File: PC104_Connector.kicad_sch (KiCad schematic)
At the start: 2 parts

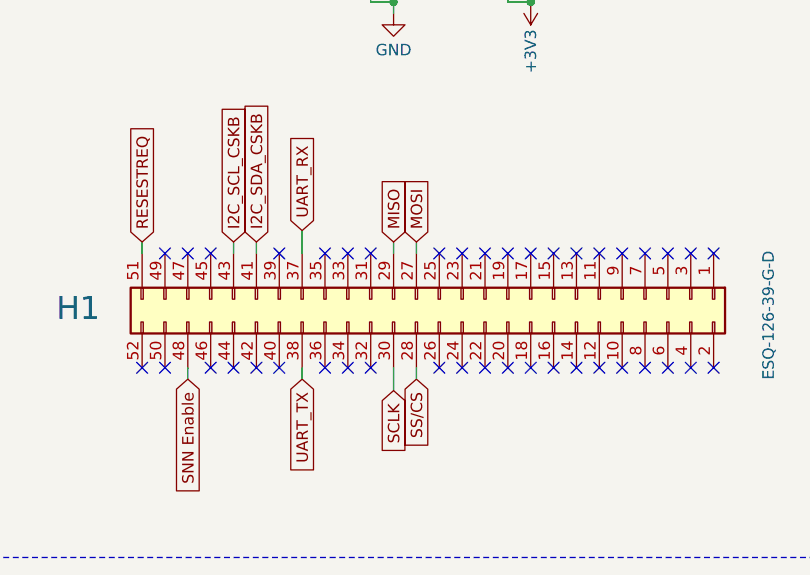
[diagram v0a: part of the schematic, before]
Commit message: Removed SPI Connections
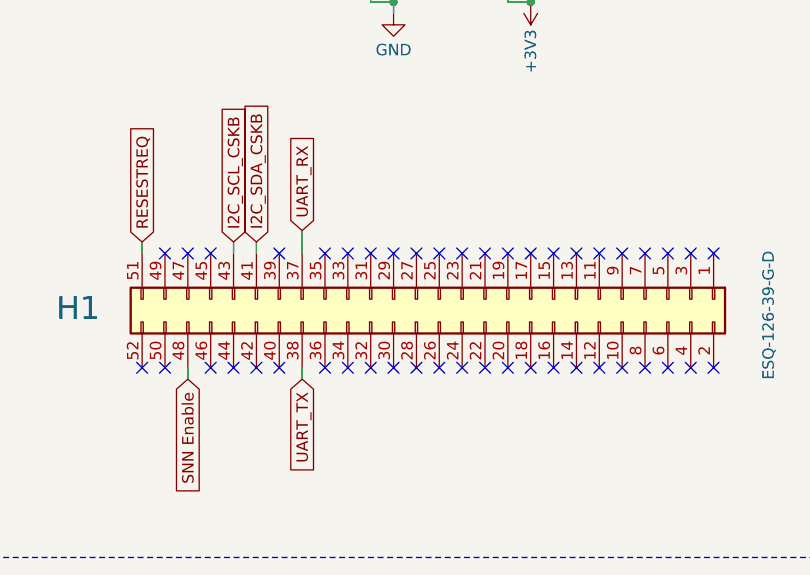
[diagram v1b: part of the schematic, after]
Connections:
- net MISO: no longer names the net of H1.29 (Pin_29)
- net MOSI: no longer names the net of H1.27 (Pin_27)
- net SCLK: no longer names the net of H1.30 (Pin_30)
- net SS/CS: no longer names the net of H1.28 (Pin_28)
- no-connect marks 88 -> 92
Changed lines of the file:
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@@
+	)
+	(no_connect
+		(at 149.86 100.33)
 	)
 	(no_connect
@@
 	)
 	(no_connect
+		(at 149.86 113.03)
+	)
+	(no_connect
 		(at 175.26 58.42)
 	)
@@
 	)
 	(no_connect
+		(at 147.32 113.03)
+	)
+	(no_connect
 		(at 172.72 58.42)
 	)
@@
 	)
 	(no_connect
+		(at 147.32 100.33)
+	)
+	(no_connect
 		(at 167.64 71.12)
 	)
@@
 	(wire
 		(pts
-			(xy 147.32 115.57) (xy 147.32 113.03)
-		)
-		(stroke
-			(width 0)
-			(type default)
-		)
-	)
-	(wire
-		(pts
 			(xy 132.08 99.06) (xy 132.08 100.33)
 		)
@@
 	(wire
 		(pts
-			(xy 149.86 114.3) (xy 149.86 113.03)
-		)
-		(stroke
-			(width 0)
-			(type default)
-		)
-	)
-	(wire
-		(pts
-			(xy 147.32 99.06) (xy 147.32 100.33)
-		)
-		(stroke
-			(width 0)
-			(type default)
-		)
-	)
-	(wire
-		(pts
 			(xy 137.16 97.79) (xy 137.16 100.33)
 		)
@@
 	(wire
 		(pts
-			(xy 149.86 99.06) (xy 149.86 100.33)
-		)
-		(stroke
-			(width 0)
-			(type default)
-		)
-	)
-	(wire
-		(pts
 			(xy 147.32 72.39) (xy 147.32 71.12)
 		)
@@
 		)
 	)
-	(global_label "MOSI"
-		(shape input)
-		(at 149.86 99.06 90)
+	(global_label "I2C_SDA_CSKB"
+		(shape input)
+		(at 132.08 99.06 90)
 		(fields_autoplaced yes)
 		(effects
@@
 		)
 		(property "Intersheetrefs" "${INTERSHEET_REFS}"
-			(at 149.86 91.4786 90)
+			(at 132.08 82.4677 90)
 			(effects
 				(font
@@
 		)
 	)
-	(global_label "I2C_SDA_CSKB"
-		(shape input)
-		(at 132.08 99.06 90)
+	(global_label "RESESTREQ"
+		(shape input)
+		(at 119.38 99.06 90)
 		(fields_autoplaced yes)
 		(effects
@@
 		)
 		(property "Intersheetrefs" "${INTERSHEET_REFS}"
-			(at 132.08 82.4677 90)
+			(at 119.38 85.3707 90)
 			(effects
 				(font
@@
 		)
 	)
-	(global_label "RESESTREQ"
-		(shape input)
-		(at 119.38 99.06 90)
+	(global_label "UART_RX"
+		(shape input)
+		(at 137.16 97.79 90)
 		(fields_autoplaced yes)
 		(effects
@@
 		)
 		(property "Intersheetrefs" "${INTERSHEET_REFS}"
-			(at 119.38 85.3707 90)
+			(at 137.16 86.701 90)
 			(effects
 				(font
@@
 		)
 	)
-	(global_label "UART_RX"
-		(shape input)
-		(at 137.16 97.79 90)
-		(fields_autoplaced yes)
-		(effects
-			(font
-				(size 1.27 1.27)
-			)
-			(justify left)
-		)
-		(property "Intersheetrefs" "${INTERSHEET_REFS}"
-			(at 137.16 86.701 90)
-			(effects
-				(font
-					(size 1.27 1.27)
-				)
-				(justify left)
-				(hide yes)
-			)
-		)
-	)
 	(global_label "UART_TX"
 		(shape input)
@@
 			(effects
 				(font
-					(size 1.27 1.27)
-				)
-				(justify right)
-				(hide yes)
-			)
-		)
-	)
-	(global_label "SCLK"
-		(shape input)
-		(at 147.32 115.57 270)
-		(fields_autoplaced yes)
-		(effects
-			(font
-				(size 1.27 1.27)
-			)
-			(justify right)
-		)
-		(property "Intersheetrefs" "${INTERSHEET_REFS}"
-			(at 147.32 123.3328 90)
-			(effects
-				(font
-					(size 1.27 1.27)
-				)
-				(justify right)
-				(hide yes)
-			)
-		)
-	)
-	(global_label "MISO"
-		(shape input)
-		(at 147.32 99.06 90)
-		(fields_autoplaced yes)
-		(effects
-			(font
-				(size 1.27 1.27)
-			)
-			(justify left)
-		)
-		(property "Intersheetrefs" "${INTERSHEET_REFS}"
-			(at 147.32 91.4786 90)
-			(effects
-				(font
-					(size 1.27 1.27)
-				)
-				(justify left)
-				(hide yes)
-			)
-		)
-	)
-	(global_label "SS{slash}CS"
-		(shape input)
-		(at 149.86 114.3 270)
-		(fields_autoplaced yes)
-		(effects
-			(font
-				(size 1.27 1.27)
-			)
-			(justify right)
-		)
-		(property "Intersheetrefs" "${INTERSHEET_REFS}"
-			(at 149.86 123.5142 90)
-			(effects
-				(font

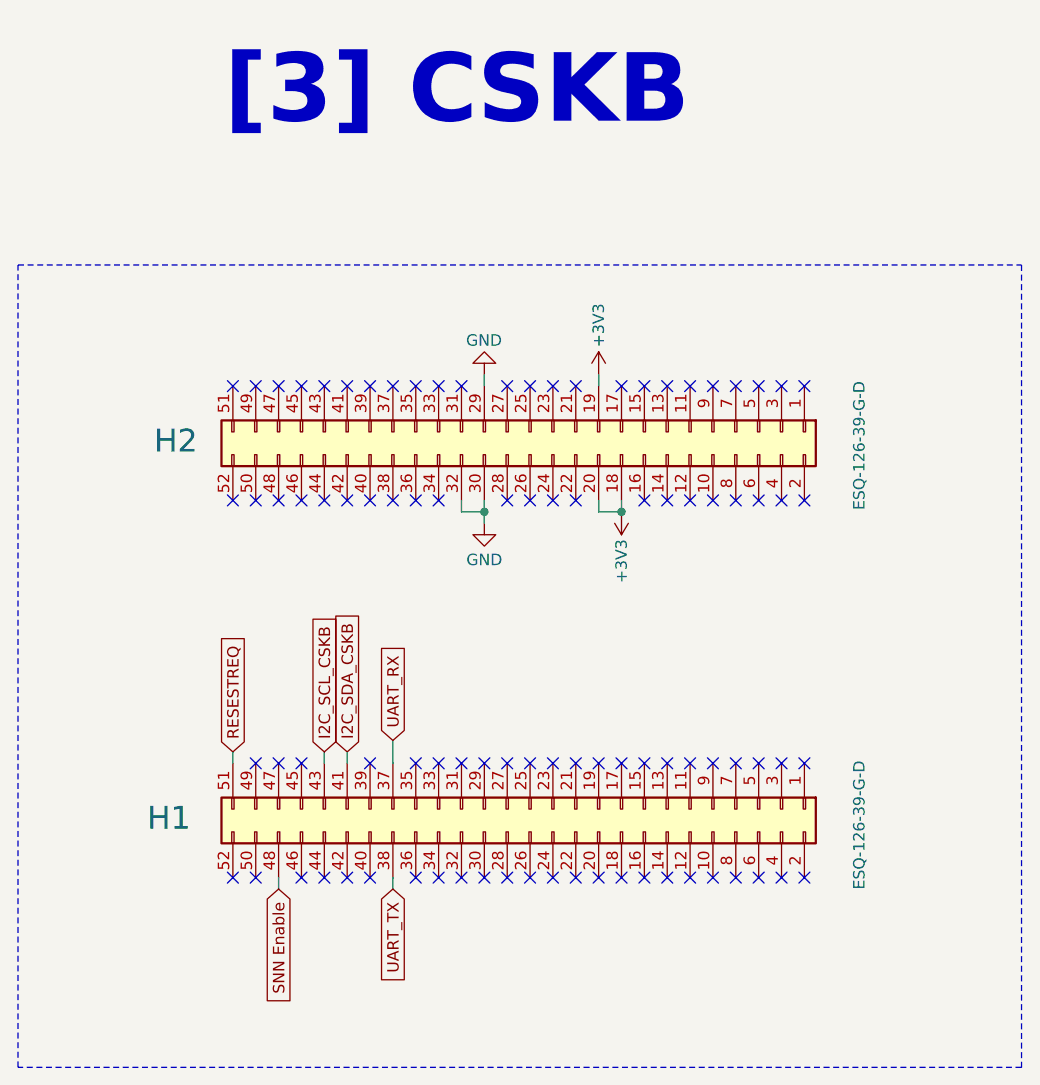
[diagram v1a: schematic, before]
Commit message: Added hierarchical lables to the schematic
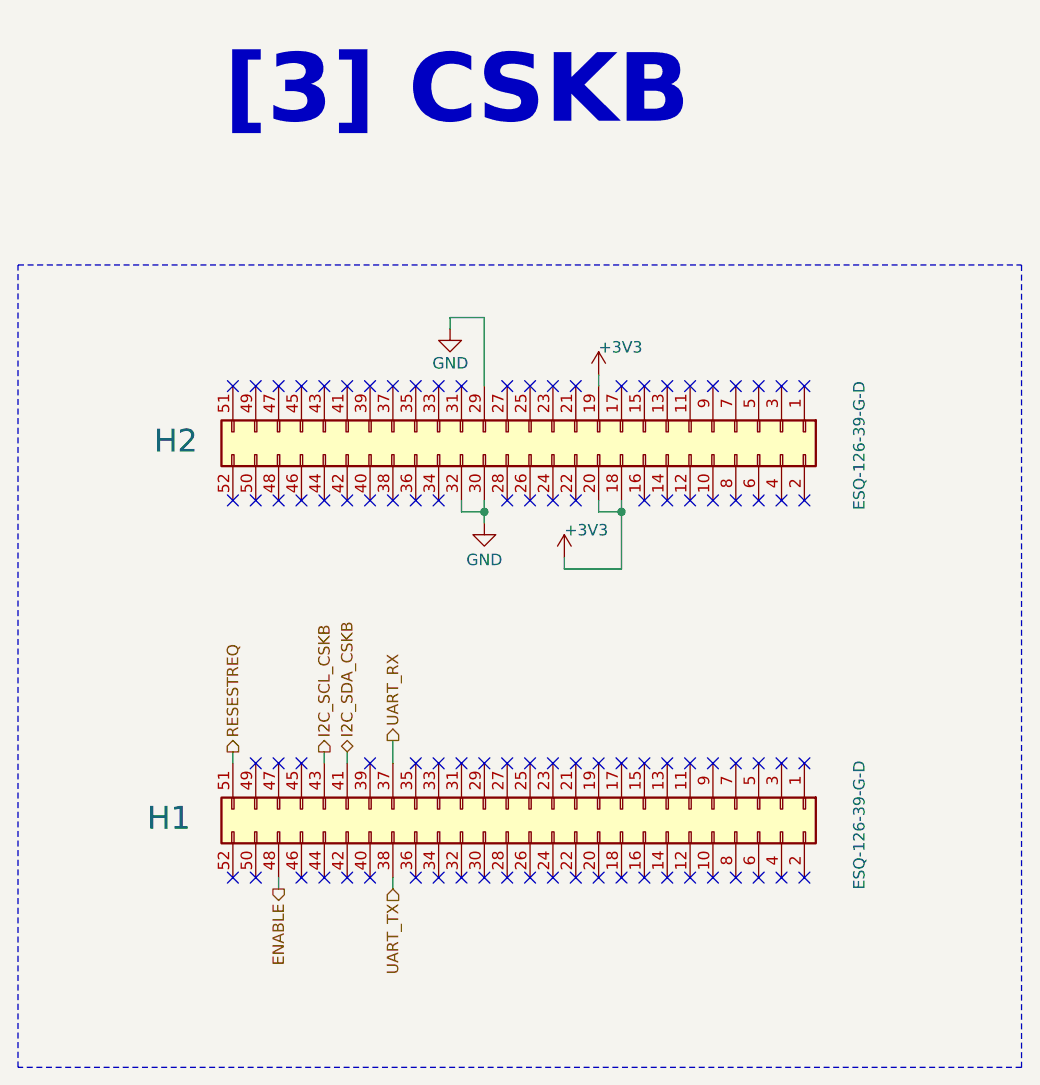
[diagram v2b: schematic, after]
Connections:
- net SNN Enable renamed ENABLE
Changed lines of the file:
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@@
+	(wire
+		(pts
+			(xy 147.32 50.8) (xy 147.32 58.42)
+		)
+		(stroke
+			(width 0)
+			(type default)
+		)
+	)
 	(wire
 		(pts
@@
 	(wire
 		(pts
+			(xy 143.51 50.8) (xy 147.32 50.8)
+		)
+		(stroke
+			(width 0)
+			(type default)
+		)
+	)
+	(wire
+		(pts
 			(xy 124.46 114.3) (xy 124.46 113.03)
 		)
@@
 	(wire
 		(pts
+			(xy 156.21 77.47) (xy 156.21 78.74)
+		)
+		(stroke
+			(width 0)
+			(type default)
+		)
+	)
+	(wire
+		(pts
 			(xy 129.54 99.06) (xy 129.54 100.33)
 		)
@@
 	(wire
 		(pts
-			(xy 147.32 57.15) (xy 147.32 58.42)
+			(xy 143.51 52.07) (xy 143.51 50.8)
 		)
 		(stroke
@@
 	(wire
 		(pts
+			(xy 162.56 78.74) (xy 162.56 72.39)
+		)
+		(stroke
+			(width 0)
+			(type default)
+		)
+	)
+	(wire
+		(pts
+			(xy 156.21 78.74) (xy 162.56 78.74)
+		)
+		(stroke
+			(width 0)
+			(type default)
+		)
+	)
+	(wire
+		(pts
 			(xy 147.32 72.39) (xy 144.78 72.39)
 		)
@@
 		)
 	)
-	(global_label "I2C_SCL_CSKB"
-		(shape input)
-		(at 129.54 99.06 90)
-		(fields_autoplaced yes)
+	(hierarchical_label "I2C_SDA_CSKB"
+		(shape bidirectional)
+		(at 132.08 99.06 90)
 		(effects
 			(font
@@
 			(justify left)
 		)
-		(property "Intersheetrefs" "${INTERSHEET_REFS}"
-			(at 129.54 82.5282 90)
-			(effects
-				(font
-					(size 1.27 1.27)
-				)
-				(justify left)
-				(hide yes)
-			)
-		)
-	)
-	(global_label "I2C_SDA_CSKB"
-		(shape input)
-		(at 132.08 99.06 90)
-		(fields_autoplaced yes)
-		(effects
-			(font
-				(size 1.27 1.27)
-			)
-			(justify left)
-		)
-		(property "Intersheetrefs" "${INTERSHEET_REFS}"
-			(at 132.08 82.4677 90)
-			(effects
-				(font
-					(size 1.27 1.27)
-				)
-				(justify left)
-				(hide yes)
-			)
-		)
-	)
-	(global_label "RESESTREQ"
-		(shape input)
-		(at 119.38 99.06 90)
-		(fields_autoplaced yes)
-		(effects
-			(font
-				(size 1.27 1.27)
-			)
-			(justify left)
-		)
-		(property "Intersheetrefs" "${INTERSHEET_REFS}"
-			(at 119.38 85.3707 90)
-			(effects
-				(font
-					(size 1.27 1.27)
-				)
-				(justify left)
-				(hide yes)
-			)
-		)
-	)
-	(global_label "UART_RX"
-		(shape input)
-		(at 137.16 97.79 90)
-		(fields_autoplaced yes)
-		(effects
-			(font
-				(size 1.27 1.27)
-			)
-			(justify left)
-		)
-		(property "Intersheetrefs" "${INTERSHEET_REFS}"
-			(at 137.16 86.701 90)
-			(effects
-				(font
-					(size 1.27 1.27)
-				)
-				(justify left)
-				(hide yes)
-			)
-		)
-	)
-	(global_label "UART_TX"
+	)
+	(hierarchical_label "UART_TX"
 		(shape input)
 		(at 137.16 114.3 270)
-		(fields_autoplaced yes)
 		(effects
 			(font
@@
 			(justify right)
 		)
-		(property "Intersheetrefs" "${INTERSHEET_REFS}"
-			(at 137.16 125.0866 90)
-			(effects
-				(font
-					(size 1.27 1.27)
-				)
-				(justify right)
-				(hide yes)
-			)
-		)
-	)
-	(global_label "SNN Enable"
-		(shape input)
+	)
+	(hierarchical_label "RESESTREQ"
+		(shape output)
+		(at 119.38 99.06 90)
+		(effects
+			(font
+				(size 1.27 1.27)
+			)
+			(justify left)
+		)
+	)
+	(hierarchical_label "I2C_SCL_CSKB"
+		(shape output)
+		(at 129.54 99.06 90)
+		(effects
+			(font
+				(size 1.27 1.27)
+			)
+			(justify left)
+		)
+	)
+	(hierarchical_label "ENABLE"
+		(shape output)
 		(at 124.46 114.3 270)
-		(fields_autoplaced yes)
 		(effects
 			(font
@@
 			(justify right)
 		)
-		(property "Intersheetrefs" "${INTERSHEET_REFS}"
-			(at 124.46 128.4731 90)
-			(effects
-				(font
-					(size 1.27 1.27)
-				)
-				(justify right)
-				(hide yes)
-			)
+	)
+	(hierarchical_label "UART_RX"
+		(shape output)
+		(at 137.16 97.79 90)
+		(effects
+			(font
+				(size 1.27 1.27)
+			)
+			(justify left)
 		)
 	)
@@
 		)
 		(property "Value" "+3V3"
-			(at 160.02 54.102 90)
+			(at 160.02 54.102 0)
 			(effects
 				(font
@@
 	(symbol
 		(lib_id "power:+3V3")
-		(at 162.56 72.39 180)
+		(at 156.21 77.47 0)
 		(unit 1)
 		(exclude_from_sim no)
@@
 		(dnp no)
 		(property "Reference" "#PWR03"
-			(at 162.56 68.58 0)
+			(at 156.21 81.28 0)
 			(effects
 				(font
@@
 		)
 		(property "Value" "+3V3"
-			(at 162.56 75.438 90)
+			(at 156.21 74.422 0)
 			(effects
 				(font
@@
 		)
 		(property "Footprint" ""
-			(at 162.56 72.39 0)
+			(at 156.21 77.47 0)
 			(effects
 				(font
@@
 		)
 		(property "Datasheet" ""
-			(at 162.56 72.39 0)
+			(at 156.21 77.47 0)
 			(effects
 				(font
@@
 		)
 		(property "Description" "Power symbol creates a global label with name \"+3V3\""
-			(at 162.56 72.39 0)
+			(at 156.21 77.47 0)
 			(effects
 				(font
@@
 	(symbol
 		(lib_id "power:GND")
-		(at 147.32 57.15 180)
+		(at 143.51 52.07 0)
 		(unit 1)
 		(exclude_from_sim no)
@@
 		(dnp no)
 		(property "Reference" "#PWR08"
-			(at 147.32 50.8 0)
+			(at 143.51 58.42 0)
 			(effects
 				(font
@@
 		)
 		(property "Value" "GND"
-			(at 145.288 53.34 0)
+			(at 145.542 55.88 0)
 			(effects
 				(font
@@
 		)
 		(property "Footprint" ""
-			(at 147.32 57.15 0)
+			(at 143.51 52.07 0)
 			(effects
 				(font
@@
 		)
 		(property "Datasheet" ""
-			(at 147.32 57.15 0)
+			(at 143.51 52.07 0)
 			(effects
 				(font
@@
 		)
 		(property "Description" "Power symbol creates a global label with name \"GND\" , ground"
-			(at 147.32 57.15 0)
-			(effects
-				(font
+			(at 143.51 52.07 0)
+			(effects
+				(font
